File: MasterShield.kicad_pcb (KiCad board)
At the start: 2 copper layers, 33 parts, among them J1 Conn_01x08_Pin, J2 Conn_01x10_Pin, J3 Conn_01x06_Pin, J4 Conn_01x08_Pin, J5 RS485, J6 Screw_Terminal_01x08, Q1 S8050, U1 MAX485E, U2 BTS724G, U3 74LVC1G08GW

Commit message: ...
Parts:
- added C4: 68uF, Capacitor_Tantalum_SMD:CP_EIA-7343-43_Kemet-X, F.Cu at (121.9, 83.8)
- added C5: 150uF, Capacitor_Tantalum_SMD:CP_EIA-7343-43_Kemet-X, F.Cu at (132.1, 68.6)
- added D3: B5817, Diode_SMD:D_SOD-323_HandSoldering, F.Cu at (133.4, 76.2)
- added L1: 100uH, Inductor_SMD:L_12x12mm_H6mm, F.Cu at (121.8, 71.1)
- added TP1: RO, TestPoint:TestPoint_Pad_D2.0mm, F.Cu at (83.8, 69.1)
- added TP2: DI, TestPoint:TestPoint_Pad_D2.0mm, F.Cu at (83.8, 73.2)
- added TP3: ~{RE}, TestPoint:TestPoint_Pad_D2.0mm, F.Cu at (83.8, 77.2)
- added TP4: DE, TestPoint:TestPoint_Pad_D2.0mm, F.Cu at (83.8, 81.3)
- added U4: LM2594M-5.0, Package_SO:SOIC-8_3.9x4.9mm_P1.27mm, F.Cu at (134.6, 81.9)
- moved J5 66.6 mm to (157.5, 101.3)
- moved U2 43.6 mm to (96.8, 88.3)
- moved J6 13.0 mm to (157.5, 68.9)

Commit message: ...
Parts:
- added D4: 10V, Diode_SMD:D_SOD-323_HandSoldering, F.Cu at (54.7, 79.6)
- added D5: SS53C, Diode_SMD:D_SOD-323_HandSoldering, F.Cu at (54.7, 82.5)
- added R17: 4.7k, Resistor_SMD:R_0805_2012Metric, F.Cu at (50.0, 79.6)
- added R20: 4.7K, Resistor_SMD:R_0805_2012Metric, F.Cu at (50.0, 82.5)
- added R21: 10K, Resistor_SMD:R_0805_2012Metric, F.Cu at (50.0, 85.5)
- added U4: LM321, Package_TO_SOT_SMD:SOT-23-5, F.Cu at (59.8, 90.5)
- added U5: LM2596S-5, Package_TO_SOT_SMD:TO-263-5_TabPin3, F.Cu at (57.0, 68.3)
- C4: value 68uF -> 680uF; footprint Capacitor_Tantalum_SMD:CP_EIA-7343-43_Kemet-X -> Capacitor_SMD:CP_Elec_10x10.5
- C5: value 150uF -> 220uF; footprint Capacitor_Tantalum_SMD:CP_EIA-7343-43_Kemet-X -> Capacitor_Tantalum_SMD:CP_EIA-7343-15_Kemet-W_Pad2.25x2.55mm_HandSolder
- D3: value B5817 -> SS53C
- L1: value 100uH -> 33uH; footprint Inductor_SMD:L_12x12mm_H6mm -> Inductor_SMD:L_Abracon_ASPI-0630LR

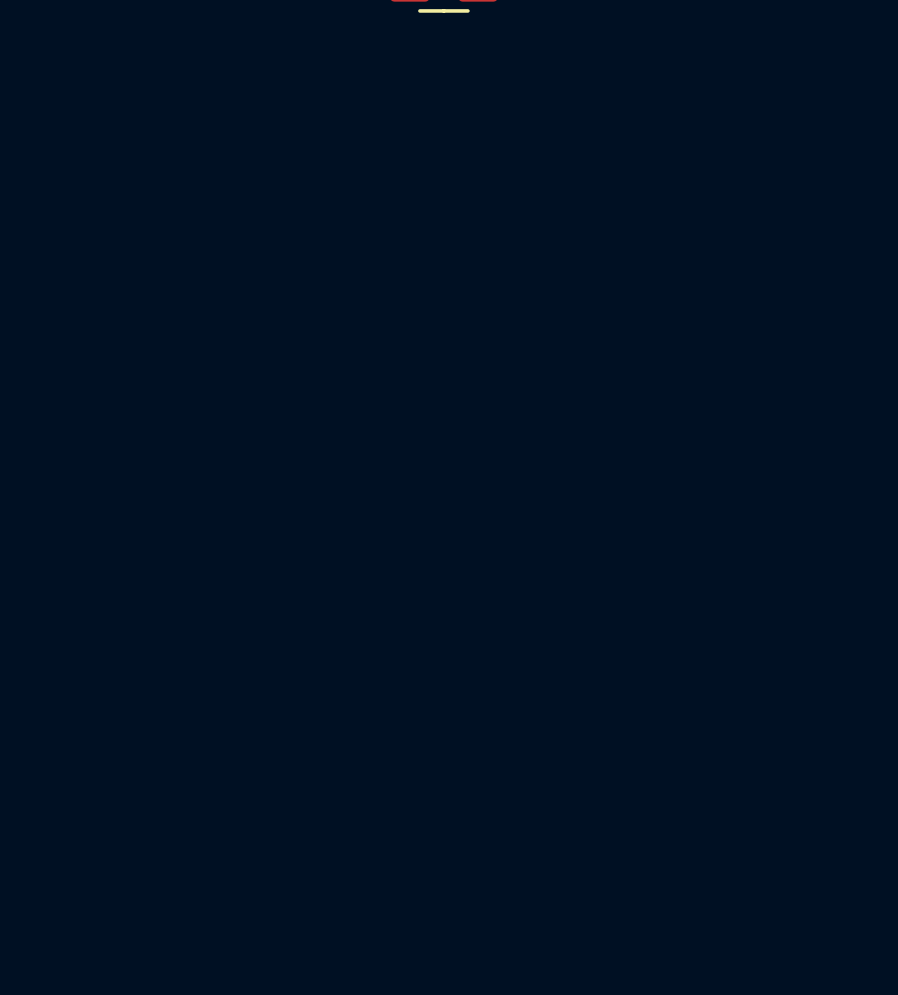
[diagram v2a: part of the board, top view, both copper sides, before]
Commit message: Added OV/UV/RP protection
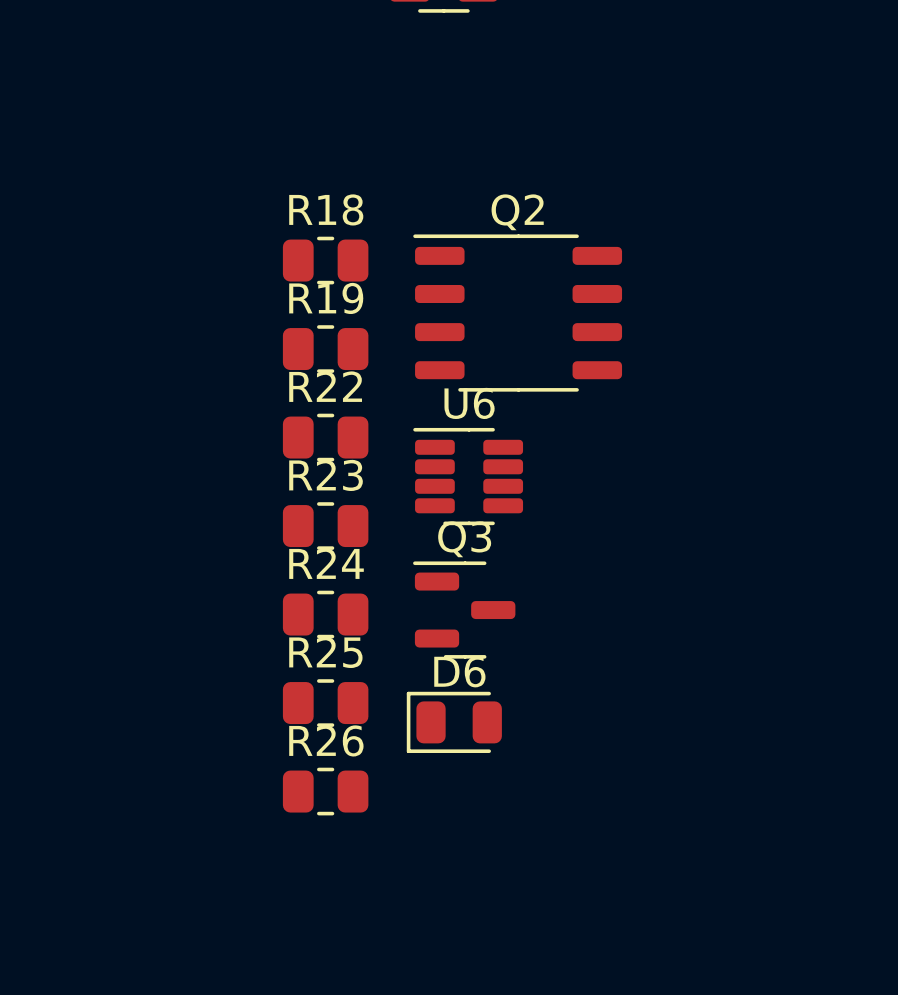
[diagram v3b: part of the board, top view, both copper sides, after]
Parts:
- added D6: LED, LED_SMD:LED_0805_2012Metric, F.Cu at (60.3, 115.8)
- added Q2: Si9945AEY-T1, Package_SO:SOP-8_3.9x4.9mm_P1.27mm, F.Cu at (62.3, 102.1)
- added Q3: S8050, Package_TO_SOT_SMD:SOT-23, F.Cu at (60.5, 112.0)
- added R18: 2700k, Resistor_SMD:R_0805_2012Metric, F.Cu at (55.9, 100.4)
- added R19: 82k, Resistor_SMD:R_0805_2012Metric, F.Cu at (55.9, 103.3)
- added R22: 82k, Resistor_SMD:R_0805_2012Metric, F.Cu at (55.9, 106.3)
- added R23: 100k, Resistor_SMD:R_0805_2012Metric, F.Cu at (55.9, 109.2)
- added R24: 1K, Resistor_SMD:R_0805_2012Metric, F.Cu at (55.9, 112.2)
- added R25: 100k, Resistor_SMD:R_0805_2012Metric, F.Cu at (55.9, 115.1)
- added R26: 4.7K, Resistor_SMD:R_0805_2012Metric, F.Cu at (55.9, 118.1)
- added U6: LTC4365TS8, Package_TO_SOT_SMD:TSOT-23-8, F.Cu at (60.7, 107.6)
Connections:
- R12 pad 2: /P0.09 -> /AD5
- R13 pad 2: /P0.08 -> /AD4
- U2 pad 4: /P0.08 -> /AD4
- U2 pad 8: /P0.09 -> /AD5

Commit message: ...
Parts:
- added J7: BATT, TerminalBlock_4Ucon:TerminalBlock_4Ucon_1x04_P3.50mm_Horizontal, F.Cu at (160.0, 135.6)
- added TP10: FUGA, TestPoint:TestPoint_Pad_D2.0mm, F.Cu at (38.1, 103.2)
- added TP11: POWER_EN4, TestPoint:TestPoint_Pad_D2.0mm, F.Cu at (38.1, 107.2)
- added TP12: POWER_EN3, TestPoint:TestPoint_Pad_D2.0mm, F.Cu at (38.1, 111.3)
- added TP13: POWER_EN2, TestPoint:TestPoint_Pad_D2.0mm, F.Cu at (38.1, 115.3)
- added TP14: POWER_EN1, TestPoint:TestPoint_Pad_D2.0mm, F.Cu at (38.1, 119.4)
- added TP15: POWER_ST12, TestPoint:TestPoint_Pad_D2.0mm, F.Cu at (42.1, 103.2)
- added TP16: POWER_ST34, TestPoint:TestPoint_Pad_D2.0mm, F.Cu at (42.1, 107.2)
- added TP17: GATE, TestPoint:TestPoint_Pad_D2.0mm, F.Cu at (42.1, 111.3)
- added TP5: UV, TestPoint:TestPoint_Pad_D2.0mm, F.Cu at (34.0, 103.2)
- added TP6: OV, TestPoint:TestPoint_Pad_D2.0mm, F.Cu at (34.0, 107.2)
- added TP7: SHDN, TestPoint:TestPoint_Pad_D2.0mm, F.Cu at (34.0, 111.3)
- added TP8: FAULT, TestPoint:TestPoint_Pad_D2.0mm, F.Cu at (34.0, 115.3)
- added TP9: FUEL_GAUGE, TestPoint:TestPoint_Pad_D2.0mm, F.Cu at (34.0, 119.4)

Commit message: ...
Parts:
- removed the C1 at (87.3, 105.5)
- removed the R2 at (78.5, 108.4)
- removed the U4 at (134.6, 81.9)
- J1: value Conn_01x08_Pin -> CONTROL/SERIAL
- J2: value Conn_01x10_Pin -> MISC
- J3: value Conn_01x06_Pin -> ADC/SENSE
- J4: value Conn_01x08_Pin -> POWER
- moved J1 167.0 mm to (251.5, 101.6), turned to 0 degrees
- moved J2 155.2 mm to (251.5, 80.0), turned to 0 degrees
- moved R21 135.8 mm to (160.0, 165.1)
- moved R20 132.3 mm to (156.2, 161.3)
- moved TP6 132.3 mm to (153.7, 50.8)
- moved TP8 130.8 mm to (148.6, 52.1)
- moved TP9 130.3 mm to (151.1, 176.5)
- moved J3 130.2 mm to (203.2, 88.9), turned to 180 degrees
- moved D4 129.6 mm to (148.6, 168.9)
- moved R17 127.0 mm to (146.1, 162.6)
- moved D5 125.3 mm to (151.1, 162.6)
- moved TP17 125.0 mm to (148.6, 45.7)
- moved U4 123.6 mm to (155.1, 169.2)
- moved TP10 123.6 mm to (143.5, 167.6)
- moved TP5 121.3 mm to (142.2, 48.3)
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
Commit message: ...
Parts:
- removed TP11: POWER_EN4, TestPoint:TestPoint_Pad_D2.0mm
- removed TP12: POWER_EN3, TestPoint:TestPoint_Pad_D2.0mm
- removed TP13: POWER_EN2, TestPoint:TestPoint_Pad_D2.0mm
- removed TP14: POWER_EN1, TestPoint:TestPoint_Pad_D2.0mm
- removed TP15: POWER_ST12, TestPoint:TestPoint_Pad_D2.0mm
- removed TP16: POWER_ST34, TestPoint:TestPoint_Pad_D2.0mm
- D1: value LED -> RXD
- D2: value LED -> TXD
- J5: value RS485 -> RS-485
- U3: value 74LVC1G08GW -> 74LVC1G08
- moved R8 157.8 mm to (245.9, 65.5), turned to 90 degrees
- moved R7 154.0 mm to (241.3, 65.5), turned to 90 degrees
- moved Q1 152.0 mm to (232.9, 80.5), turned to -90 degrees
- moved TP3 151.1 mm to (220.7, 89.7), turned to 180 degrees
- moved TP1 150.5 mm to (217.3, 89.7), turned to 180 degrees
- moved R6 150.1 mm to (236.6, 65.5), turned to 90 degrees
- moved R2 149.7 mm to (241.3, 84.8), turned to 90 degrees
- moved R5 147.3 mm to (231.9, 65.5), turned to 90 degrees
- moved R3 143.9 mm to (227.2, 65.5), turned to 90 degrees
- moved R11 143.9 mm to (236.6, 84.8), turned to 90 degrees
- moved TP4 143.3 mm to (213.7, 89.7), turned to 180 degrees
- moved U1 141.2 mm to (233.6, 72.3), turned to 90 degrees
- moved R16 141.0 mm to (245.9, 75.4), turned to -90 degrees
- moved C3 140.9 mm to (227.2, 71.2), turned to 90 degrees
- moved R1 140.1 mm to (217.9, 71.1), turned to -90 degrees
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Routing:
- net +5V: track 0.00 -> 51.7 mm, vias 0 -> 6
- net Net-(D3-K): track 0.00 -> 23.0 mm
- net Net-(J5-Pin_3): track 0.00 -> 13.6 mm
- net Net-(J5-Pin_4): track 0.00 -> 12.2 mm
- net Net-(U1-~{RE}): track 0.00 -> 10.7 mm
- net +12V: track 0.00 -> 8.27 mm
- net Net-(U1-DE): track 0.00 -> 7.57 mm
- net Net-(D1-K): track 0.00 -> 5.95 mm
- net Net-(D2-K): track 0.00 -> 5.83 mm
- net Net-(U1-B): track 0.00 -> 5.42 mm
- net Net-(U1-A): track 0.00 -> 5.35 mm
- net Net-(R15-Pad2): track 0.00 -> 4.58 mm
- net /AD5: track 0.00 -> 4.57 mm
- net /AD4: track 0.00 -> 4.57 mm
- net /ENA: track 0.00 -> 3.23 mm
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- added copper zone on In1.Cu, net +5V
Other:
- copper layers 2 -> 4

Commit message: ...
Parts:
- J5: value RS-485 -> RS485
- U3: value 74LVC1G08 -> 74LVC1G08GW
- moved U2 136.8 mm to (242.4, 91.2), turned to 180 degrees
- moved C4 127.6 mm to (234.7, 107.2)
- moved D3 127.6 mm to (225.2, 106.9)
- moved U5 127.6 mm to (223.3, 119.6)
- moved C5 127.6 mm to (223.9, 102.5)
- moved L1 127.6 mm to (233.4, 119.5)
- moved TP10 119.8 mm to (221.4, 76.6)
- moved U4 114.4 mm to (211.7, 69.8)
- moved R20 111.6 mm to (212.1, 64.6)
- moved R21 111.1 mm to (207.5, 64.6), turned to 180 degrees
- moved D4 110.9 mm to (206.9, 74.5), turned to 90 degrees
- moved R17 108.6 mm to (211.1, 75.6)
- moved D5 108.5 mm to (206.9, 69.5), turned to 90 degrees
- moved TP9 106.5 mm to (208.5, 86.9), turned to 180 degrees
- moved R12 103.1 mm to (207.6, 98.4), turned to 90 degrees
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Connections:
- C3 pad 1: GND -> +5V
- C3 pad 2: +5V -> GND
- J5 pad 1: +5V -> Net-(J5-Pin_1)
- J6 pad 7: Net-(J6-Pin_7) -> Net-(J5-Pin_1)
- R12 pad 2: /AD5 -> /AD4
- R13 pad 2: /AD4 -> /AD5
- U2 pad 13: Net-(J6-Pin_7) -> Net-(J5-Pin_1)
- U2 pad 4: /AD4 -> /AD5
- U2 pad 8: /AD5 -> /AD4
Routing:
- net GND: track 1.82 -> 343.6 mm, vias 25 -> 38
- net +5V: track 51.7 -> 164.5 mm, vias 6 -> 11
- net +12V: track 8.27 -> 117.6 mm, vias 0 -> 12
- net +BATT: track 0.00 -> 81.8 mm
- net /P0.01: track 0.00 -> 77.9 mm, vias 0 -> 1
- net /P0.00: track 0.00 -> 75.7 mm, vias 0 -> 1
- net Net-(J5-Pin_1): track 0.00 -> 71.9 mm, vias 0 -> 2
- net /AD5: track 4.57 -> 71.2 mm
- net Net-(U1-~{RE}): track 10.7 -> 75.2 mm
- net Net-(Q2A-G): track 0.00 -> 62.6 mm
- net /AD4: track 4.57 -> 63.3 mm
- net +3.3V: track 0.00 -> 58.1 mm
- net /P0.08: track 0.00 -> 52.9 mm, vias 0 -> 2
- net Net-(J6-Pin_2): track 0.00 -> 43.9 mm
- net /ENA: track 3.23 -> 45.8 mm
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- added copper zone on In2.Cu, net GND

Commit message: ...
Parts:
- added J8: RS485 A, TerminalBlock_4Ucon:TerminalBlock_4Ucon_1x04_P3.50mm_Horizontal, F.Cu at (219.1, 59.2)
- added REF**: MountingHole_2.5mm_Pad, MountingHole:MountingHole_2.5mm_Pad, F.Cu at (200.7, 132.1)
- added REF**: MountingHole_2.5mm_Pad, MountingHole:MountingHole_2.5mm_Pad, F.Cu at (254.0, 132.1)
- added REF**: MountingHole_2.5mm_Pad, MountingHole:MountingHole_2.5mm_Pad, F.Cu at (200.7, 50.8)
- added REF**: MountingHole_2.5mm_Pad, MountingHole:MountingHole_2.5mm_Pad, F.Cu at (254.0, 50.8)
- J5: value RS485 -> RS485 B
- J6: value Screw_Terminal_01x08 -> EXTRA POWER; footprint TerminalBlock_4Ucon:TerminalBlock_4Ucon_1x08_P3.50mm_Horizontal -> TerminalBlock_4Ucon:TerminalBlock_4Ucon_1x04_P3.50mm_Horizontal
- R6: value R120 -> 120R
- R7: value R10 -> 10R
- moved TP3 24.9 mm to (216.7, 80.6)
- moved TP4 22.1 mm to (209.8, 80.6)
- moved TP2 22.1 mm to (213.2, 80.6)
- moved TP1 17.4 mm to (217.9, 75.8)
- moved J6 14.0 mm to (249.5, 118.6)
- moved J5 5.52 mm to (245.3, 59.2)
- moved D2 4.83 mm to (224.9, 58.9)
- moved D1 3.56 mm to (228.3, 58.9)
- moved R7 0.08 mm to (241.3, 65.6)
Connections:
- U2 pad 13: Net-(J5-Pin_1) -> Net-(J8-Pin_1)
- U2 pad 14: Net-(J6-Pin_6) -> Net-(J5-Pin_1)
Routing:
- net Net-(J8-Pin_1): track 0.00 -> 70.5 mm, vias 0 -> 2
- net Net-(J6-Pin_6): track 34.8 -> 0.00 mm
- net Net-(J5-Pin_4): track 11.4 -> 45.9 mm
- net Net-(J5-Pin_1): track 71.9 -> 41.5 mm
- net Net-(J5-Pin_3): track 14.3 -> 42.6 mm
- net Net-(U1-~{RE}): track 75.2 -> 49.1 mm, vias 0 -> 2
- net Net-(J6-Pin_2): track 43.9 -> 28.7 mm
- net Net-(J6-Pin_3): track 41.5 -> 27.8 mm
- net Net-(U1-DE): track 48.8 -> 36.8 mm
- net /P0.00: track 75.7 -> 69.6 mm, vias 1 -> 3
- net /P0.01: track 77.9 -> 82.9 mm, vias 1 -> 3
- net Net-(D2-K): track 5.83 -> 10.6 mm
- net GND: track 343.6 -> 340.0 mm
- net Net-(D1-K): track 5.95 -> 9.33 mm
- net /P0.08: track 52.9 -> 55.6 mm
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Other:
- board outline added: 63.5 x 91.4 mm
